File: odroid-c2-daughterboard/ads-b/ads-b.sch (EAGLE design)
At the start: 38 parts, among them U1 SEN-09403, U3 BMP180

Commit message: Updates from first schem review
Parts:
- added R17, R18, R19: 0, rcl:R-US_R0603
- R12, R301, R302: value 10K -> 1K
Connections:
- new net N$11: R17.2, U4.AD0
- new net N$12: R18.2, U4.FSYNC
- new net N$13: R19.2, U4.CLKIN
- net CO2_AD: now also JP3.1
- net GND: now also R17.1, R18.1, R19.1
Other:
- note added: "Daughterboard for ODROID-C2"
- note added: "I2C Address = 0x68"
- note added: "ODROID-C2 40-pin Header"
- note added: "UART default baud rate 38.4kbps"
- note added: "u-blox CAM-M8Q"
- note removed: "I2C Address = 0x69"
- note removed: "Intended for ODROID-C2"
- moved on the sheet: C3, C4
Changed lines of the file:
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@@
 <part name="FRAME101" library="titleblock" deviceset="REDLINE-COVER-TITLEBLOCK" device=""/>
 <part name="TB301" library="titleblock" deviceset="REDLINE-TITLEBLOCK" device=""/>
-<part name="R301" library="rcl" deviceset="R-US_" device="R0603" value="10K"/>
+<part name="R301" library="rcl" deviceset="R-US_" device="R0603" value="1K"/>
 <part name="LED301" library="led" deviceset="LED" device="SML0603"/>
 <part name="GND302" library="supply1" deviceset="GND" device=""/>
-<part name="R302" library="rcl" deviceset="R-US_" device="R0603" value="10K"/>
+<part name="R302" library="rcl" deviceset="R-US_" device="R0603" value="1K"/>
 <part name="LED302" library="led" deviceset="LED" device="SML0603"/>
 <part name="GND304" library="supply1" deviceset="GND" device=""/>
@@
 <part name="Q2" library="transistor-power" deviceset="P-MOSFET-SO8" device=""/>
 <part name="R11" library="rcl" deviceset="R-US_" device="R0603" value="220"/>
-<part name="R12" library="rcl" deviceset="R-US_" device="R0603" value="10K"/>
+<part name="R12" library="rcl" deviceset="R-US_" device="R0603" value="1K"/>
 <part name="LED1" library="led" deviceset="LED" device="SML0603"/>
 <part name="GND13" library="supply1" deviceset="GND" device=""/>
@@
 <part name="R6" library="rcl" deviceset="R-US_" device="R0603" value="10K"/>
 <part name="GND18" library="supply1" deviceset="GND" device=""/>
+<part name="R17" library="rcl" deviceset="R-US_" device="R0603" value="0"/>
+<part name="GND19" library="supply1" deviceset="GND" device=""/>
+<part name="R18" library="rcl" deviceset="R-US_" device="R0603" value="0"/>
+<part name="GND20" library="supply1" deviceset="GND" device=""/>
+<part name="R19" library="rcl" deviceset="R-US_" device="R0603" value="0"/>
+<part name="GND21" library="supply1" deviceset="GND" device=""/>
 </parts>
 <sheets>
@@
 <text x="235.204" y="31.75" size="2.54" layer="100">0.1</text>
 <text x="10.16" y="198.12" size="7.62" layer="100">ADS-B Receiver</text>
-<text x="10.16" y="190.5" size="2.54" layer="100">Intended for ODROID-C2</text>
+<text x="10.16" y="190.5" size="2.54" layer="100">Daughterboard for ODROID-C2</text>
 <text x="10.16" y="162.56" size="3.048" layer="100">Pages</text>
 <text x="10.16" y="157.48" size="2.54" layer="100">1.  SOM and Power Header</text>
@@
 <text x="63.5" y="86.36" size="1.778" layer="100">SOC controls shutdown via KEEP_ALIVE</text>
 <text x="30.48" y="83.82" size="1.778" layer="100">SOC monitors SWITCH_MONITOR to watch when user switches off power and then perform graceful shutdown</text>
+<text x="170.18" y="93.98" size="1.778" layer="100">ODROID-C2 40-pin Header</text>
 </plain>
 <instances>
@@
 </segment>
 </net>
+<net name="CO2_AD" class="0">
+<segment>
+<pinref part="JP3" gate="A" pin="1"/>
+<wire x1="187.96" y1="119.38" x2="228.6" y2="119.38" width="0.1524" layer="91"/>
+<label x="228.6" y="119.38" size="1.778" layer="95" rot="MR0"/>
+</segment>
+</net>
 </nets>
 </sheet>
@@
 <plain>
 <text x="119.38" y="200.66" size="5.08" layer="100">GPS Receiver</text>
+<text x="116.84" y="106.68" size="1.778" layer="100">u-blox CAM-M8Q</text>
+<text x="106.68" y="104.14" size="1.778" layer="100">UART default baud rate 38.4kbps</text>
 </plain>
 <instances>
@@
 Cut-off around ~340Hz</text>
 <text x="86.36" y="50.8" size="1.778" layer="100">BMP180</text>
-<text x="121.92" y="116.84" size="1.778" layer="100">I2C Address = 0x69</text>
+<text x="121.92" y="116.84" size="1.778" layer="100">I2C Address = 0x68</text>
 <text x="121.92" y="114.3" size="1.778" layer="100">Max 400kHz</text>
 <text x="78.74" y="48.26" size="1.778" layer="100">I2C Address = 0xEF</text>
@@
 <instance part="U4" gate="G$1" x="134.62" y="142.24"/>
 <instance part="+3V3" gate="G$1" x="114.3" y="180.34"/>
-<instance part="GND7" gate="1" x="114.3" y="124.46"/>
+<instance part="GND7" gate="1" x="114.3" y="121.92"/>
 <instance part="C1" gate="G$1" x="109.22" y="170.18"/>
 <instance part="GND8" gate="1" x="109.22" y="162.56"/>
-<instance part="C3" gate="G$1" x="99.06" y="132.08"/>
-<instance part="GND9" gate="1" x="99.06" y="124.46"/>
-<instance part="C4" gate="G$1" x="106.68" y="132.08"/>
-<instance part="GND10" gate="1" x="106.68" y="124.46"/>
+<instance part="C3" gate="G$1" x="78.74" y="132.08"/>
+<instance part="GND9" gate="1" x="78.74" y="121.92"/>
+<instance part="C4" gate="G$1" x="88.9" y="132.08"/>
+<instance part="GND10" gate="1" x="88.9" y="121.92"/>
 <instance part="+3V13" gate="G$1" x="109.22" y="93.98"/>
 <instance part="C5" gate="G$1" x="116.84" y="86.36"/>
@@
 <instance part="C7" gate="G$1" x="172.72" y="58.42"/>
 <instance part="GND17" gate="1" x="172.72" y="50.8"/>
+<instance part="R17" gate="G$1" x="165.1" y="127" rot="R90"/>
+<instance part="GND19" gate="1" x="165.1" y="119.38"/>
+<instance part="R18" gate="G$1" x="99.06" y="129.54" rot="R90"/>
+<instance part="GND20" gate="1" x="99.06" y="121.92"/>
+<instance part="R19" gate="G$1" x="106.68" y="129.54" rot="R90"/>
+<instance part="GND21" gate="1" x="106.68" y="121.92"/>
 </instances>
 <busses>
@@
 <pinref part="U4" gate="G$1" pin="GND@17"/>
 <wire x1="114.3" y1="132.08" x2="114.3" y2="129.54" width="0.1524" layer="91"/>
-<wire x1="114.3" y1="129.54" x2="114.3" y2="127" width="0.1524" layer="91"/>
+<wire x1="114.3" y1="129.54" x2="114.3" y2="124.46" width="0.1524" layer="91"/>
 <wire x1="116.84" y1="132.08" x2="114.3" y2="132.08" width="0.1524" layer="91"/>
 <junction x="114.3" y="132.08"/>
@@
 <pinref part="GND10" gate="1" pin="GND"/>
 <pinref part="C4" gate="G$1" pin="2"/>
+<wire x1="88.9" y1="127" x2="88.9" y2="124.46" width="0.1524" layer="91"/>
 </segment>
 <segment>
 <pinref part="GND9" gate="1" pin="GND"/>
 <pinref part="C3" gate="G$1" pin="2"/>
+<wire x1="78.74" y1="127" x2="78.74" y2="124.46" width="0.1524" layer="91"/>
 </segment>
 <segment>
@@
 <pinref part="C7" gate="G$1" pin="2"/>
 <pinref part="GND17" gate="1" pin="GND"/>
+</segment>
+<segment>
+<pinref part="GND19" gate="1" pin="GND"/>
+<pinref part="R17" gate="G$1" pin="1"/>
+</segment>
+<segment>
+<pinref part="R18" gate="G$1" pin="1"/>
+<pinref part="GND20" gate="1" pin="GND"/>
+</segment>
+<segment>
+<pinref part="R19" gate="G$1" pin="1"/>
+<pinref part="GND21" gate="1" pin="GND"/>
 </segment>
 </net>
@@
 <pinref part="C3" gate="G$1" pin="1"/>
 <pinref part="U4" gate="G$1" pin="REGOUT"/>
-<wire x1="116.84" y1="147.32" x2="99.06" y2="147.32" width="0.1524" layer="91"/>
-<wire x1="99.06" y1="147.32" x2="99.06" y2="134.62" width="0.1524" layer="91"/>
+<wire x1="116.84" y1="147.32" x2="78.74" y2="147.32" width="0.1524" layer="91"/>
+<wire x1="78.74" y1="147.32" x2="78.74" y2="134.62" width="0.1524" layer="91"/>
 </segment>
 </net>
@@
 <pinref part="C4" gate="G$1" pin="1"/>
 <pinref part="U4" gate="G$1" pin="CPOUT"/>
-<wire x1="116.84" y1="144.78" x2="106.68" y2="144.78" width="0.1524" layer="91"/>
-<wire x1="106.68" y1="144.78" x2="106.68" y2="134.62" width="0.1524" layer="91"/>
+<wire x1="116.84" y1="144.78" x2="88.9" y2="144.78" width="0.1524" layer="91"/>
+<wire x1="88.9" y1="144.78" x2="88.9" y2="134.62" width="0.1524" layer="91"/>
 </segment>
 </net>
@@
 </segment>
 </net>
+<net name="N$11" class="0">
+<segment>
+<pinref part="U4" gate="G$1" pin="AD0"/>
+<pinref part="R17" gate="G$1" pin="2"/>
+<wire x1="152.4" y1="144.78" x2="165.1" y2="144.78" width="0.1524" layer="91"/>
+<wire x1="165.1" y1="144.78" x2="165.1" y2="132.08" width="0.1524" layer="91"/>
+</segment>
+</net>
+<net name="N$12" class="0">
+<segment>
+<pinref part="U4" gate="G$1" pin="FSYNC"/>
+<pinref part="R18" gate="G$1" pin="2"/>
+<wire x1="116.84" y1="139.7" x2="99.06" y2="139.7" width="0.1524" layer="91"/>
+<wire x1="99.06" y1="139.7" x2="99.06" y2="134.62" width="0.1524" layer="91"/>
+</segment>
+</net>
+<net name="N$13" class="0">
+<segment>
+<pinref part="U4" gate="G$1" pin="CLKIN"/>
+<pinref part="R19" gate="G$1" pin="2"/>
+<wire x1="116.84" y1="137.16" x2="106.68" y2="137.16" width="0.1524" layer="91"/>
+<wire x1="106.68" y1="137.16" x2="106.68" y2="134.62" width="0.1524" layer="91"/>
+</segment>
+</net>
 </nets>
 </sheet>
 </sheets>
+<errors>
+</errors>
 </schematic>
 </drawing>

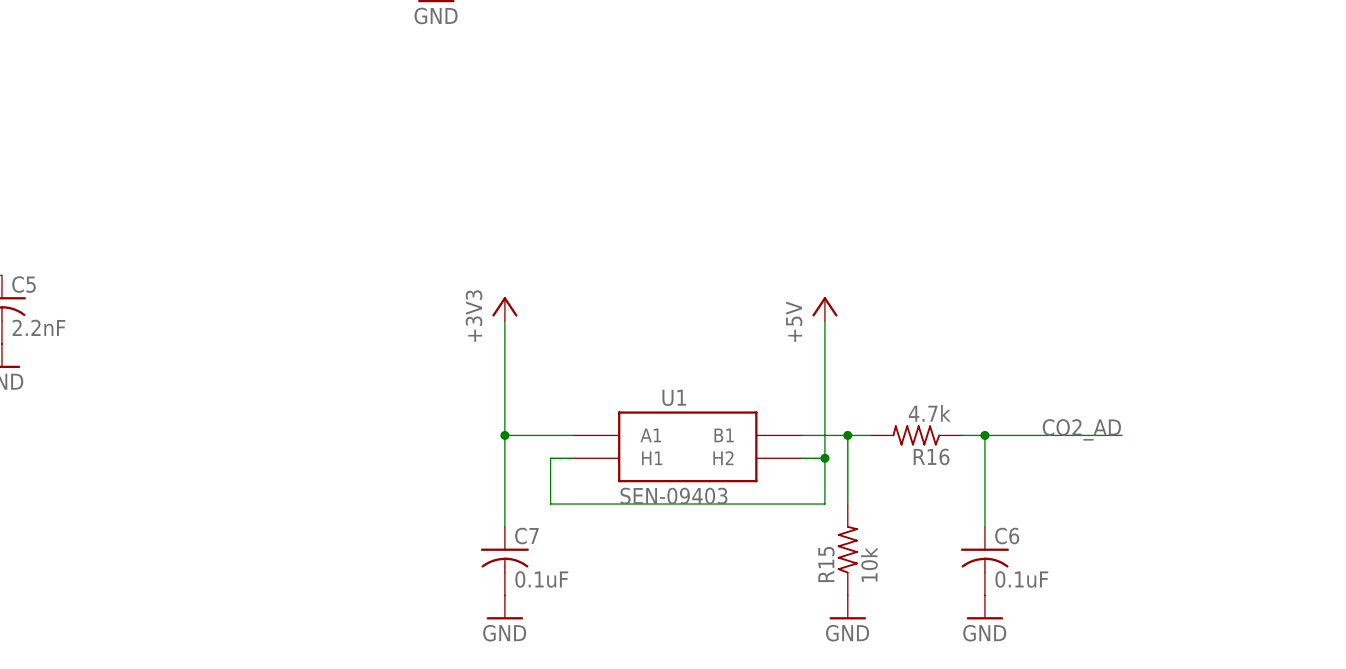
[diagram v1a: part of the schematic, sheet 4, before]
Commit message: Fix ODROID-C2 board outline, add pull-ups for FETs
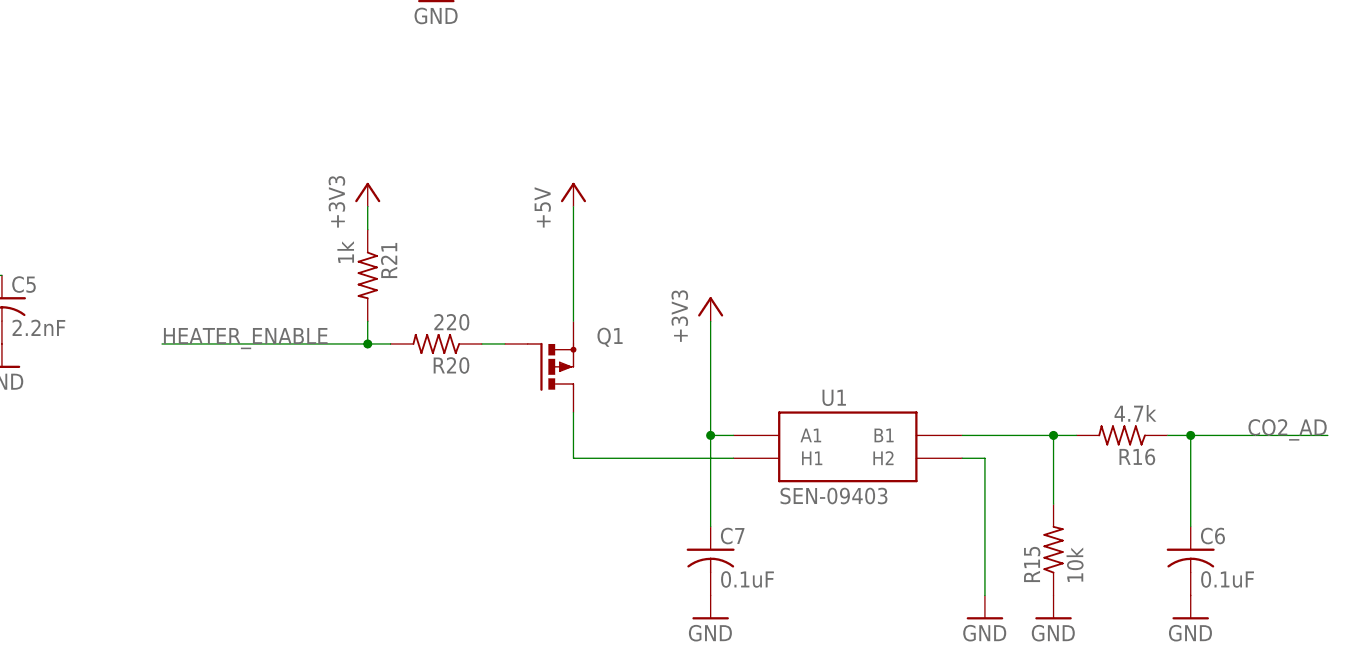
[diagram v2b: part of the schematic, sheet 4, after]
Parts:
- added Q1: (no value), transistor-power:P-MOSFET-SO8
- added R20: 220, rcl:R-US_R0603
- added R21: 1k, rcl:R-US_R0603
- added R22, R23: 10K, rcl:R-US_R0603
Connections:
- new net HEATER_ENABLE: R20.2, R21.2
- new net N$14: Q1.D, U1.H1
- new net N$16: Q1.G, R20.1
- net +3V3: now also R21.1
- net +5V: now also Q1.S; no longer U1.H1, U1.H2
- net GND: now also R23.1, U1.H2
- net N$7: now also R22.2
- net N$9: now also R22.1, R23.2
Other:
- moved on the sheet: C6, C7, JP4, JP5, R11, R15, R16, S2, U1

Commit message: ADS-B board sloppily laid out
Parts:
- removed R13: 4.7k, rcl:R-US_R0603
- removed R7, R8: 10k, rcl:R-US_R0603
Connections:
- net +3V3: no longer R7.2, R8.2
- net +5V: now also S2.S; no longer S2.O
- net GND: no longer JP3.27, R13.1
- net HEATER_ENABLE: now also JP3.34
- net I2CB_SCL: no longer R8.1
- net I2CB_SDA: no longer R7.1
- net KEEP_ALIVE: no longer R13.2
- net N$10: now also S2.O; no longer S2.S
- net N$2: now also B2.+1; no longer B2.+
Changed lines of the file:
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@@
 <part name="GND11" library="supply1" deviceset="GND" device=""/>
 <part name="GND12" library="supply1" deviceset="GND" device=""/>
-<part name="R7" library="rcl" deviceset="R-US_" device="R0603" value="10k"/>
-<part name="R8" library="rcl" deviceset="R-US_" device="R0603" value="10k"/>
-<part name="+3V14" library="supply1" deviceset="+3V3" device=""/>
-<part name="+3V15" library="supply1" deviceset="+3V3" device=""/>
 <part name="+3V4" library="supply1" deviceset="+3V3" device=""/>
 <part name="+3V5" library="supply1" deviceset="+3V3" device=""/>
@@
 <part name="LED1" library="led" deviceset="LED" device="SML0603"/>
 <part name="GND13" library="supply1" deviceset="GND" device=""/>
-<part name="R13" library="rcl" deviceset="R-US_" device="R0603" value="4.7k"/>
-<part name="GND14" library="supply1" deviceset="GND" device=""/>
 <part name="R14" library="rcl" deviceset="R-US_" device="R0603" value="4.7k"/>
 <part name="+3V8" library="supply1" deviceset="+3V3" device=""/>
@@
 <instance part="JP4" gate="G$1" x="60.96" y="144.78" rot="R180"/>
 <instance part="JP5" gate="G$1" x="60.96" y="111.76" rot="R180"/>
-<instance part="P+1" gate="1" x="109.22" y="152.4"/>
+<instance part="P+1" gate="1" x="109.22" y="157.48"/>
 <instance part="GND1" gate="1" x="88.9" y="106.68"/>
 <instance part="P+2" gate="1" x="195.58" y="185.42"/>
@@
 <instance part="LED1" gate="G$1" x="116.84" y="27.94"/>
 <instance part="GND13" gate="1" x="116.84" y="15.24"/>
-<instance part="R13" gate="G$1" x="208.28" y="111.76" rot="R90"/>
-<instance part="GND14" gate="1" x="208.28" y="101.6"/>
 <instance part="R5" gate="G$1" x="119.38" y="129.54" rot="R90"/>
 <instance part="R6" gate="G$1" x="119.38" y="114.3" rot="R90"/>
@@
 </segment>
 <segment>
-<pinref part="JP3" gate="A" pin="27"/>
-<wire x1="187.96" y1="152.4" x2="195.58" y2="152.4" width="0.1524" layer="91"/>
-<wire x1="195.58" y1="152.4" x2="195.58" y2="144.78" width="0.1524" layer="91"/>
 <pinref part="JP3" gate="A" pin="35"/>
 <wire x1="195.58" y1="144.78" x2="195.58" y2="132.08" width="0.1524" layer="91"/>
@@
 <wire x1="195.58" y1="127" x2="195.58" y2="104.14" width="0.1524" layer="91"/>
 <wire x1="187.96" y1="162.56" x2="195.58" y2="162.56" width="0.1524" layer="91"/>
-<wire x1="195.58" y1="162.56" x2="195.58" y2="152.4" width="0.1524" layer="91"/>
+<wire x1="195.58" y1="162.56" x2="195.58" y2="144.78" width="0.1524" layer="91"/>
 <pinref part="JP3" gate="A" pin="21"/>
 <wire x1="187.96" y1="144.78" x2="195.58" y2="144.78" width="0.1524" layer="91"/>
@@
 <wire x1="187.96" y1="127" x2="195.58" y2="127" width="0.1524" layer="91"/>
 <pinref part="GND3" gate="1" pin="GND"/>
-<junction x="195.58" y="152.4"/>
 <junction x="195.58" y="144.78"/>
 <junction x="195.58" y="132.08"/>
@@
 <pinref part="GND13" gate="1" pin="GND"/>
 <wire x1="116.84" y1="22.86" x2="116.84" y2="17.78" width="0.1524" layer="91"/>
-</segment>
-<segment>
-<pinref part="R13" gate="G$1" pin="1"/>
-<pinref part="GND14" gate="1" pin="GND"/>
-<wire x1="208.28" y1="106.68" x2="208.28" y2="104.14" width="0.1524" layer="91"/>
 </segment>
 <segment>
@@
 </segment>
 <segment>
-<pinref part="S2" gate="1" pin="O"/>
 <pinref part="P+1" gate="1" pin="+5V"/>
-<wire x1="101.6" y1="147.32" x2="109.22" y2="147.32" width="0.1524" layer="91"/>
-<wire x1="109.22" y1="147.32" x2="109.22" y2="149.86" width="0.1524" layer="91"/>
-<wire x1="109.22" y1="119.38" x2="109.22" y2="147.32" width="0.1524" layer="91"/>
+<wire x1="109.22" y1="119.38" x2="109.22" y2="142.24" width="0.1524" layer="91"/>
 <pinref part="Q2" gate="G$1" pin="D"/>
+<wire x1="109.22" y1="142.24" x2="109.22" y2="154.94" width="0.1524" layer="91"/>
 <wire x1="88.9" y1="121.92" x2="88.9" y2="119.38" width="0.1524" layer="91"/>
 <wire x1="88.9" y1="119.38" x2="109.22" y2="119.38" width="0.1524" layer="91"/>
-<junction x="109.22" y="147.32"/>
+<pinref part="S2" gate="1" pin="S"/>
+<wire x1="101.6" y1="142.24" x2="109.22" y2="142.24" width="0.1524" layer="91"/>
+<junction x="109.22" y="142.24"/>
 </segment>
 </net>
@@
 <segment>
 <pinref part="JP3" gate="A" pin="29"/>
-<wire x1="187.96" y1="154.94" x2="208.28" y2="154.94" width="0.1524" layer="91"/>
 <label x="228.6" y="154.94" size="1.778" layer="95" rot="MR0"/>
-<pinref part="R13" gate="G$1" pin="2"/>
-<wire x1="208.28" y1="154.94" x2="228.6" y2="154.94" width="0.1524" layer="91"/>
-<wire x1="208.28" y1="116.84" x2="208.28" y2="154.94" width="0.1524" layer="91"/>
-<junction x="208.28" y="154.94"/>
+<wire x1="187.96" y1="154.94" x2="228.6" y2="154.94" width="0.1524" layer="91"/>
 </segment>
 </net>
@@
 <net name="N$10" class="0">
 <segment>
-<pinref part="S2" gate="1" pin="S"/>
 <pinref part="R5" gate="G$1" pin="2"/>
-<wire x1="101.6" y1="142.24" x2="119.38" y2="142.24" width="0.1524" layer="91"/>
-<wire x1="119.38" y1="142.24" x2="119.38" y2="134.62" width="0.1524" layer="91"/>
+<wire x1="119.38" y1="147.32" x2="119.38" y2="134.62" width="0.1524" layer="91"/>
+<pinref part="S2" gate="1" pin="O"/>
+<wire x1="101.6" y1="147.32" x2="119.38" y2="147.32" width="0.1524" layer="91"/>
 </segment>
 </net>
@@
 <wire x1="187.96" y1="119.38" x2="228.6" y2="119.38" width="0.1524" layer="91"/>
 <label x="228.6" y="119.38" size="1.778" layer="95" rot="MR0"/>
+</segment>
+</net>
+<net name="HEATER_ENABLE" class="0">
+<segment>
+<pinref part="JP3" gate="A" pin="34"/>
+<wire x1="180.34" y1="160.02" x2="137.16" y2="160.02" width="0.1524" layer="91"/>
+<label x="137.16" y="160.02" size="1.778" layer="95"/>
 </segment>
 </net>
@@
 <segment>
 <pinref part="U$2" gate="G$1" pin="8/V_BCKUP"/>
-<pinref part="B2" gate="G$1" pin="+"/>
-<wire x1="147.32" y1="142.24" x2="170.18" y2="142.24" width="0.1524" layer="91"/>
-<wire x1="170.18" y1="142.24" x2="170.18" y2="109.22" width="0.1524" layer="91"/>
+<wire x1="147.32" y1="142.24" x2="175.26" y2="142.24" width="0.1524" layer="91"/>
+<pinref part="B2" gate="G$1" pin="+1"/>
+<wire x1="175.26" y1="109.22" x2="175.26" y2="142.24" width="0.1524" layer="91"/>
 </segment>
 </net>
@@
 <instance part="GND11" gate="1" x="116.84" y="78.74"/>
 <instance part="GND12" gate="1" x="109.22" y="58.42"/>
-<instance part="R7" gate="G$1" x="66.04" y="78.74" rot="R90"/>
-<instance part="R8" gate="G$1" x="73.66" y="78.74" rot="R90"/>
-<instance part="+3V14" gate="G$1" x="66.04" y="86.36"/>
-<instance part="+3V15" gate="G$1" x="73.66" y="86.36"/>
 <instance part="U1" gate="G$1" x="210.82" y="68.58"/>
 <instance part="R15" gate="G$1" x="233.68" y="58.42" rot="R90"/>
@@
 </segment>
 <segment>
-<pinref part="R7" gate="G$1" pin="2"/>
-<pinref part="+3V14" gate="G$1" pin="+3V3"/>
-</segment>
-<segment>
-<pinref part="R8" gate="G$1" pin="2"/>
-<pinref part="+3V15" gate="G$1" pin="+3V3"/>
-</segment>
-<segment>
 <pinref part="U1" gate="G$1" pin="A1"/>
 <wire x1="195.58" y1="71.12" x2="195.58" y2="83.82" width="0.1524" layer="91"/>
@@
 <segment>
 <pinref part="U3" gate="G$1" pin="SDA"/>
-<wire x1="76.2" y1="71.12" x2="66.04" y2="71.12" width="0.1524" layer="91"/>
 <label x="48.26" y="71.12" size="1.778" layer="95"/>
-<pinref part="R7" gate="G$1" pin="1"/>
-<wire x1="66.04" y1="71.12" x2="48.26" y2="71.12" width="0.1524" layer="91"/>
-<wire x1="66.04" y1="73.66" x2="66.04" y2="71.12" width="0.1524" layer="91"/>
-<junction x="66.04" y="71.12"/>
+<wire x1="76.2" y1="71.12" x2="48.26" y2="71.12" width="0.1524" layer="91"/>
 </segment>
 </net>
@@
 <segment>
 <pinref part="U3" gate="G$1" pin="SCL"/>
-<wire x1="76.2" y1="66.04" x2="73.66" y2="66.04" width="0.1524" layer="91"/>
 <label x="48.26" y="66.04" size="1.778" layer="95"/>
-<pinref part="R8" gate="G$1" pin="1"/>
-<wire x1="73.66" y1="66.04" x2="48.26" y2="66.04" width="0.1524" layer="91"/>
-<wire x1="73.66" y1="73.66" x2="73.66" y2="66.04" width="0.1524" layer="91"/>
-<junction x="73.66" y="66.04"/>
-</segment>
-</net>
+<wire x1="76.2" y1="66.04" x2="48.26" y2="66.04" width="0.1524" layer="91"/>
+</segment>
+</net>
